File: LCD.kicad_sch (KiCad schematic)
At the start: 2 parts

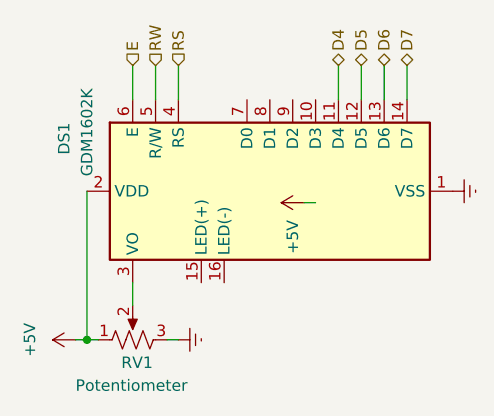
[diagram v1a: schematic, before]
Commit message: added pot for audio volume
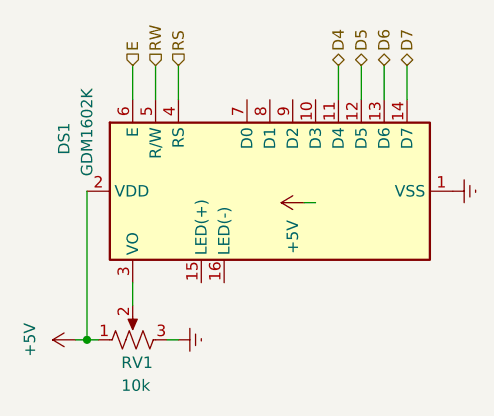
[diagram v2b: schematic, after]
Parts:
- RV1: value Potentiometer -> 10k
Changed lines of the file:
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@@
       (effects (font (size 1.27 1.27)) (justify right))
     )
-    (property "Value" "Potentiometer" (at 110.49 116.84 90)
+    (property "Value" "10k" (at 115.57 116.84 90)
       (effects (font (size 1.27 1.27)) (justify right))
     )
